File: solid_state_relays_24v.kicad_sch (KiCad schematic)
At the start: 65 parts, among them J1 1190297, J2 1190297, J3 1190297, J4 1190297, J5 1190297, J6 1190297, J7 1190297, J8 1190297, Q1 IRF4905PBF, Q2 IRF4905PBF, Q3 IRF4905PBF, Q4 IRF4905PBF, Q5 IRF4905PBF, Q6 IRF4905PBF, Q7 IRF4905PBF, Q8 IRF4905PBF

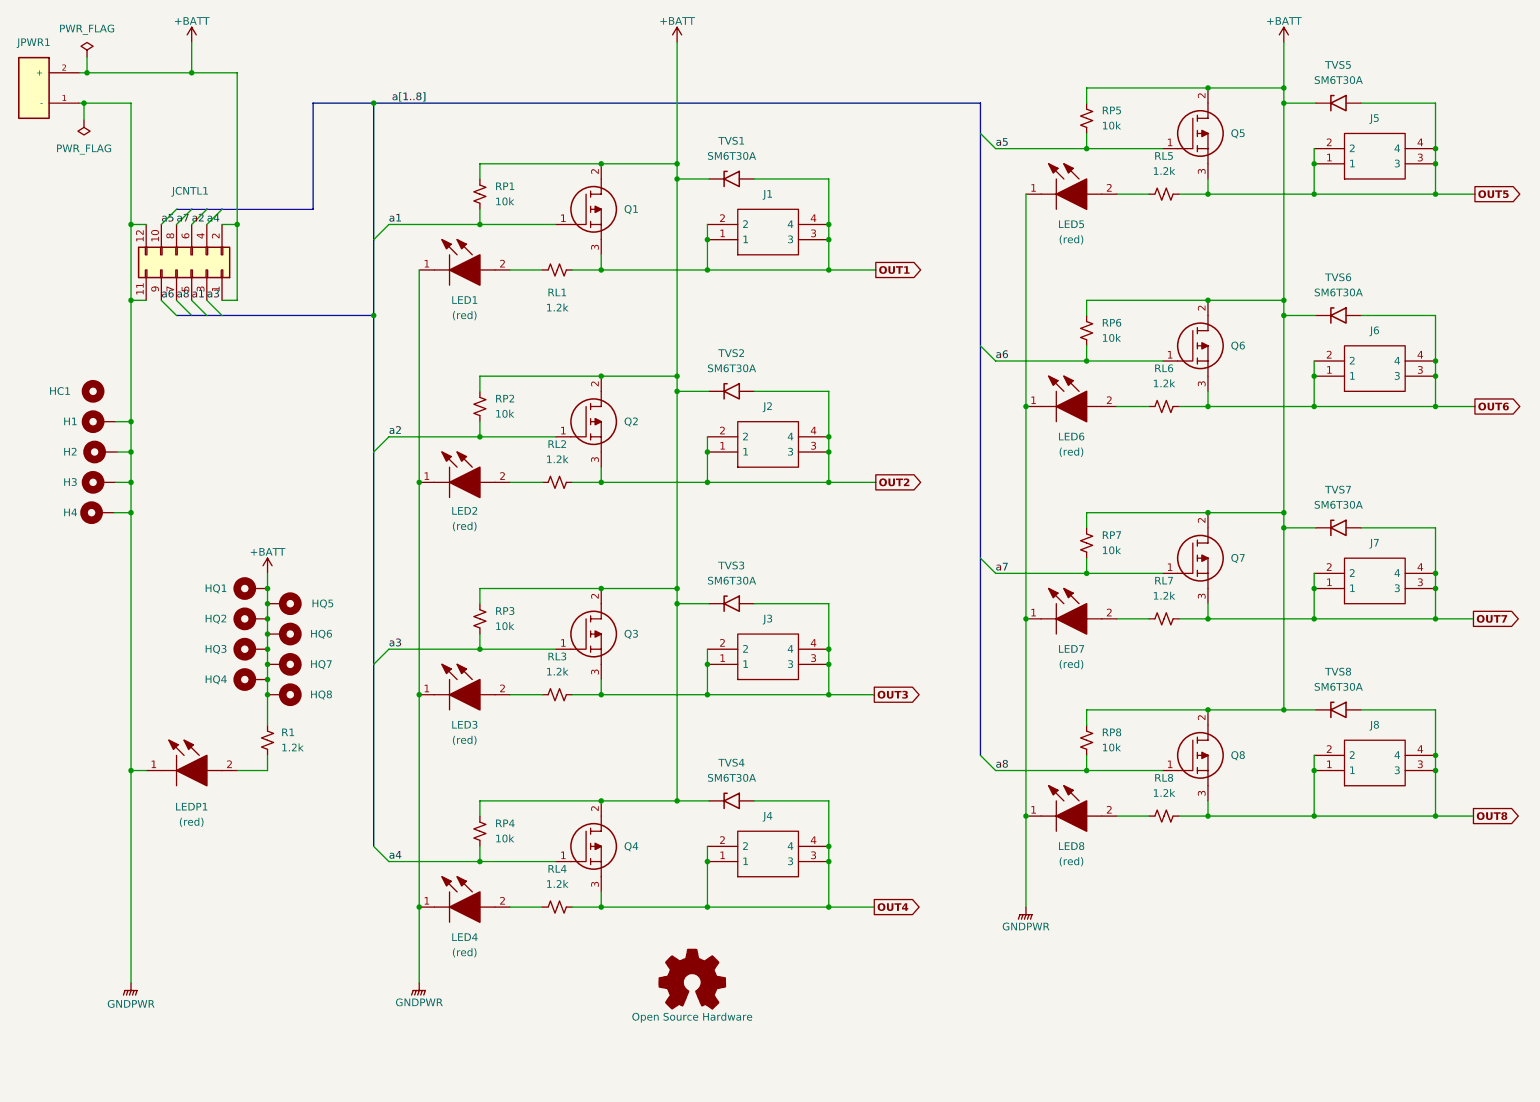
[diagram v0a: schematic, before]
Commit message: Total redo on schematic for v0.0.8
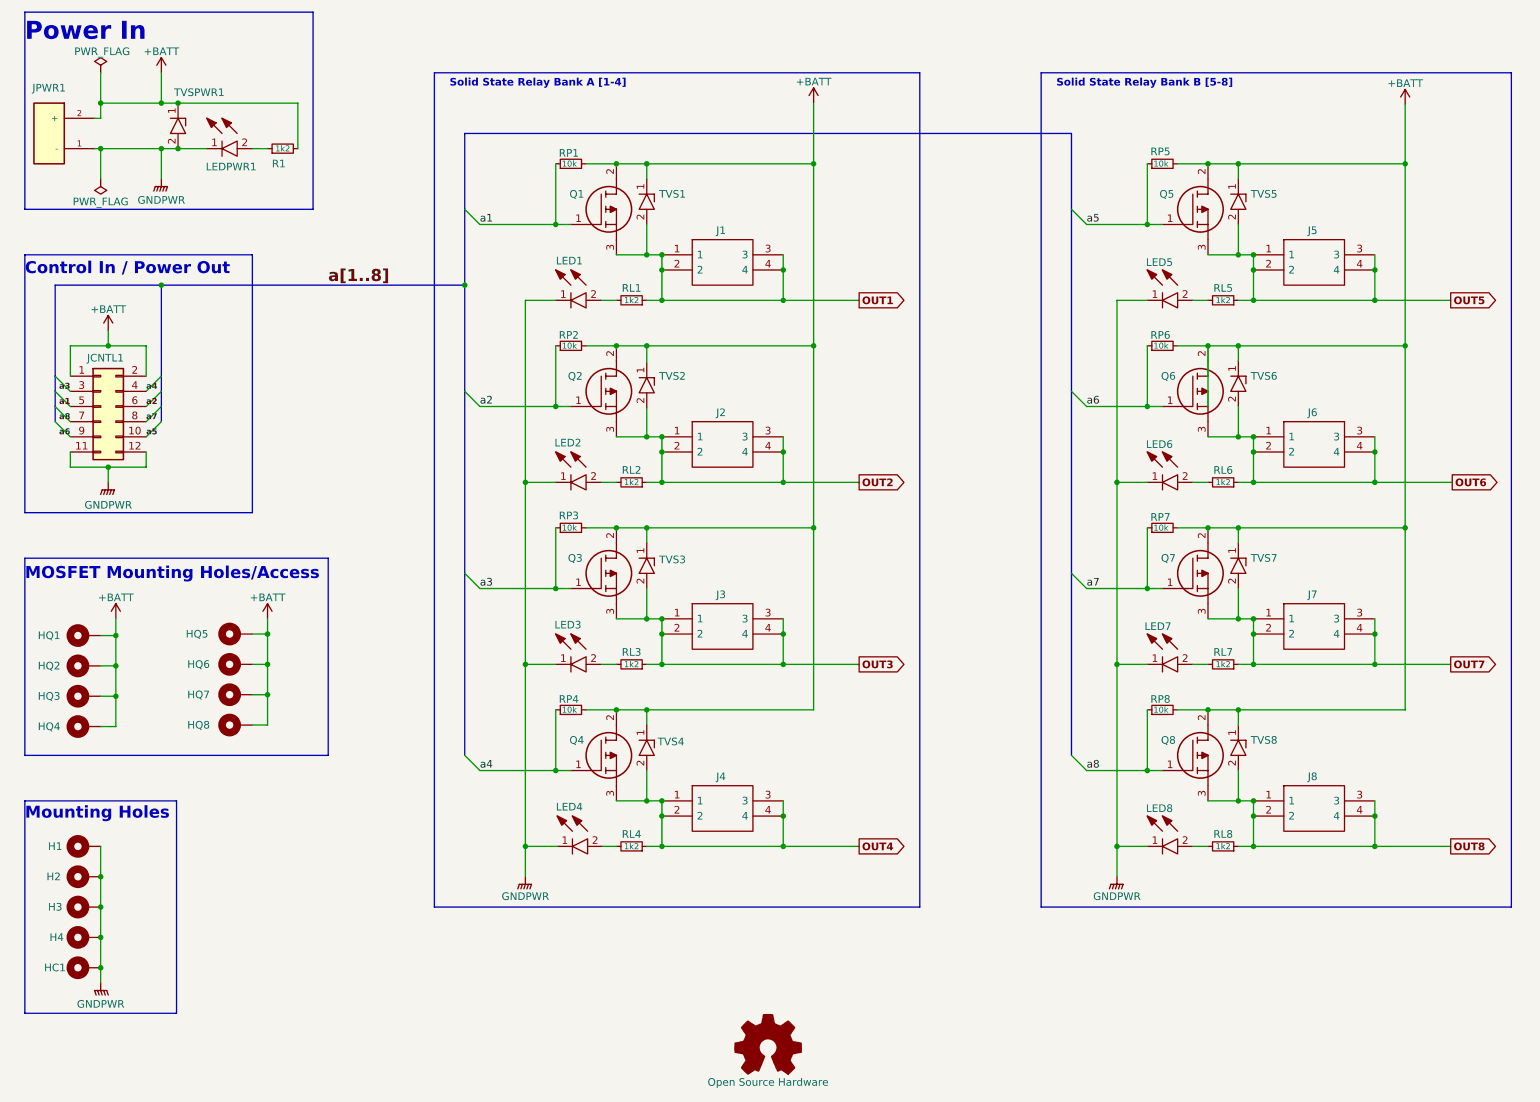
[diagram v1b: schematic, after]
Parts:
- removed J2, J3, J4, J5, J6, J7, J8: 1190297, Connector_Pheonix_Other:1190297, symbol SamacSys_Parts:1190297
- removed LED2, LED3, LED4, LED5, LED6, LED7, LED8, LEDP1: (red), SamacSys_Parts:LEDC2012X120N, symbol SamacSys_Parts:LTST-C170KRKT
- removed R1, RL2, RL3, RL4, RL5, RL6, RL7, RL8: 1.2k, Resistor_SMD:R_0805_2012Metric, symbol Device:R_Small_US
- removed RP2, RP3, RP4, RP5, RP6, RP7, RP8: 10k, Resistor_SMD:R_0805_2012Metric, symbol Device:R_Small_US
- removed TVS2, TVS3, TVS4, TVS5, TVS6, TVS7, TVS8: SM6T30A, Diode_SMD:D_SMB, symbol Diode:SM6T30A
- added J2, J3, J4, J5, J6, J7, J8: 1190297, dragon_mobile:1190297, symbol dragon_mobile:1190297
- added LED2, LED3, LED4, LED5, LED6, LED7, LED8: LTST-C190KFKT, dragon_mobile:LEDC1607X80N, symbol dragon_mobile:LTST-C190KFKT
- added LEDPWR1: LTST-C190KGKT, dragon_mobile:LEDC1608X80N, symbol dragon_mobile:LTST-C190KGKT
- added R1: 1k2, Resistor_SMD:R_0603_1608Metric_Pad0.98x0.95mm_HandSolder, symbol Device:R_Small
- added RL2, RL3, RL4, RL5, RL6, RL7, RL8: 1k2, Resistor_SMD:R_0805_2012Metric, symbol Device:R_Small
- added RP2, RP3, RP4, RP5, RP6, RP7, RP8: 10k, Resistor_SMD:R_0805_2012Metric, symbol Device:R_Small
- added TVS2, TVS3, TVS4, TVS5, TVS6, TVS7, TVS8, TVSPWR1: SM6T30AY, dragon_mobile:SMBJ36CATR, symbol dragon_mobile:SM6T30AY
- HC1: symbol Mechanical:MountingHole -> Mechanical:MountingHole_Pad
- J1: footprint Connector_Pheonix_Other:1190297 -> dragon_mobile:1190297; symbol SamacSys_Parts:1190297 -> dragon_mobile:1190297
- JCNTL1: MPN 78207-106HLF -> 78207-1012HLF; Mouser Part Number 649-78207-106HLF -> 649-78207-112HLF
- JPWR1: footprint Dragon:Amass_XT60PW-M_Kombifootprint -> dragon_mobile:Amass_XT60PW-M_Kombifootprint
- LED1: value (red) -> LTST-C190KFKT; footprint SamacSys_Parts:LEDC2012X120N -> dragon_mobile:LEDC1607X80N; symbol SamacSys_Parts:LTST-C170KRKT -> dragon_mobile:LTST-C190KFKT; Height 1.2 -> 0.8; Manufacturer_Part_Number LTST-C170KRKT -> LTST-C190KFKT; Mouser Part Number 859-LTST-C170KRKT -> 859-LTST-C190KFKT; Mouser Price/Stock https://www.mouser.com/ProductDetail/Lite-On/LTST-C170KRKT?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 -> https://www.mouser.com/ProductDetail/Lite-On/LTST-C190KFKT?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
- Q1, Q2, Q3, Q4, Q5, Q6, Q7, Q8: footprint SamacSys_Parts:TO254P469X1042X1967-3P -> dragon_mobile:TO254P469X1042X1967-3P
- RL1: value 1.2k -> 1k2; symbol Device:R_Small_US -> Device:R_Small
- RP1: symbol Device:R_Small_US -> Device:R_Small
- TVS1: value SM6T30A -> SM6T30AY; footprint Diode_SMD:D_SMB -> dragon_mobile:SMBJ36CATR; symbol Diode:SM6T30A -> dragon_mobile:SM6T30AY; Height (none) -> 2.65; Manufacturer_Name (none) -> STMicroelectronics; Manufacturer_Part_Number (none) -> SM6T30AY; Mouser Part Number (none) -> 511-SM6T30AY; Mouser Price/Stock (none) -> https://www.mouser.com/ProductDetail/STMicroelectronics/SM6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
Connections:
- net +BATT: now also RP1.2, R1.2, RP2.2, RP3.2, RP4.2, RP5.2, RP6.2, RP7.2, RP8.2, TVS2.1, TVS3.1, TVS4.1, TVS5.1, TVS6.1, TVS7.1, TVS8.1, TVSPWR1.1; no longer RP1.1
- net GNDPWR: now also HC1.1, LED2.1, LED3.1, LED4.1, LED5.1, LED6.1, LED7.1, LED8.1, LEDPWR1.1, TVSPWR1.2
- net OUT1: now also RL1.1; no longer RL1.2
- net OUT2: now also J2.1, J2.2, J2.3, J2.4, RL2.1, TVS2.2
- net OUT3: now also J3.1, J3.2, J3.3, J3.4, RL3.1, TVS3.2
- net OUT4: now also J4.1, J4.2, J4.3, J4.4, RL4.1, TVS4.2
- net OUT5: now also J5.1, J5.2, J5.3, J5.4, RL5.1, TVS5.2
- net OUT6: now also J6.1, J6.2, J6.3, J6.4, RL6.1, TVS6.2
- net OUT7: now also J7.1, J7.2, J7.3, J7.4, RL7.1, TVS7.2
- net OUT8: now also J8.1, J8.2, J8.3, J8.4, RL8.1, TVS8.2
- net a1: now also RP1.1; no longer RP1.2
- net a2: now also RP2.1
- net a3: now also RP3.1
- net a4: now also RP4.1
- net a5: now also RP5.1
- net a6: now also RP6.1
- net a7: now also RP7.1
- net a8: now also RP8.1
- net at LED1.2: now also RL1.2; no longer RL1.1
- new net: LED2.2, RL2.2
- new net: LED3.2, RL3.2
- new net: LED6.2, RL6.2
- new net: LED8.2, RL8.2
- new net: LED5.2, RL5.2
- new net: LEDPWR1.2, R1.1
- new net: LED7.2, RL7.2
- new net: LED4.2, RL4.2
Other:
- note added: "Control In / Power Out"
- note added: "MOSFET Mounting Holes/Access"
- note added: "Mounting Holes"
- note added: "Power In"
- note added: "Solid State Relay Bank A [1-4]"
- note added: "Solid State Relay Bank B [5-8]"
- moved on the sheet: H1, H2, H3, H4, HQ1, HQ2, HQ3, HQ4, HQ5, HQ6, HQ7, HQ8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

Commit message: Updating schematic and PCB for v0.0.8
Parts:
- renumbered LEDPWR1 to LEDP1, TVSPWR1 to TVSP1
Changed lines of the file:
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@@
   (symbol (lib_id "dragon_mobile:SM6T30AY") (at 40.894 30.48 270) (unit 1)
     (in_bom yes) (on_board yes)
-    (property "Reference" "TVSPWR1" (id 0) (at 44.45 28.702 90))
+    (property "Reference" "TVSP1" (id 0) (at 44.45 28.702 90))
     (property "Value" "SM6T30AY" (id 1) (at 43.434 30.48 0)
       (effects (font (size 1.27 1.27)) (justify left) hide)
@@
   (symbol (lib_id "dragon_mobile:LTST-C190KGKT") (at 45.72 38.1 0) (unit 1)
     (in_bom yes) (on_board yes)
-    (property "Reference" "LEDPWR1" (id 0) (at 49.784 41.148 0))
+    (property "Reference" "LEDP1" (id 0) (at 49.784 41.148 0))
     (property "Value" "LTST-C190KGKT" (id 1) (at 48.2346 30.48 0)
       (effects (font (size 1.27 1.27)) hide)
@@
     )
     (path "/ab793da5-b061-43cb-877a-4a6d90ef81c7"
-      (reference "LEDPWR1") (unit 1) (value "LTST-C190KGKT") (footprint "dragon_mobile:LEDC1608X80N")
+      (reference "LEDP1") (unit 1) (value "LTST-C190KGKT") (footprint "dragon_mobile:LEDC1608X80N")
     )
     (path "/1bbd3b22-5cf6-47d1-ab8c-da8e17c71421"
@@
     )
     (path "/3e9feb08-284e-450e-b0f5-20bdc79d8989"
-      (reference "TVSPWR1") (unit 1) (value "SM6T30AY") (footprint "dragon_mobile:SMBJ36CATR")
-    )
-  )
+      (reference "TVSP1") (unit 1) (value "SM6T30AY") (footprint "dragon_mobile:SMBJ36CATR")
+    )
+  )

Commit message: v0.0.10-pre2
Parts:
- added JP1: SolderJumper_2_Bridged, Jumper:SolderJumper-2_P1.3mm_Bridged_RoundedPad1.0x1.5mm, symbol Jumper:SolderJumper_2_Bridged
- added TVSP2: SM6T30AY, dragon_mobile:SMBJ36CATR, symbol dragon_mobile:SM6T30AY
- H1, H2, H3, H4, HC1, HQ1, HQ2, HQ3, HQ4, HQ5, HQ6, HQ7, HQ8: now left out of the parts list
- JPWR1: value XT60PW-M_Kombifootprint -> XT60PW-M; footprint dragon_mobile:Amass_XT60PW-M_Kombifootprint -> dragon_mobile:XT60PWM; symbol Connector_Amass_XT:XT60-M -> dragon_mobile:XT60PW-M; Height (none) -> 8.4; Manufacturer_Name (none) -> Changzou Amass Elec; Manufacturer_Part_Number (none) -> XT60PW-M; URL https://hackaday.io/page/6674-amass-xt60pw-m-combination-fo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 -> (none)
- Q1, Q2, Q3, Q4, Q5, Q6, Q7, Q8: symbol SamacSys_Parts:IRF4905PBF -> dragon_mobile:IRF4905PBF
- R1: value 1k2 -> 1k5; footprint Resistor_SMD:R_0603_1608Metric_Pad0.98x0.95mm_HandSolder -> dragon_mobile:RESC2012X65N; symbol Device:R_Small -> dragon_mobile:SDR10EZPJ152; Height (none) -> 0.65; Manufacturer_Name (none) -> ROHM Semiconductor; Manufacturer_Part_Number (none) -> SDR10EZPJ152; Mouser Part Number (none) -> 755-SDR10EZPJ152; Mouser Price/Stock (none) -> https://www.mouser.com/ProductDetail/ROHM-Semiconductor/SDR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
- RL1, RL2, RL3, RL4, RL5, RL6, RL7, RL8: value 1k2 -> 1k5; footprint Resistor_SMD:R_0805_2012Metric -> dragon_mobile:RESC2012X65N; symbol Device:R_Small -> dragon_mobile:SDR10EZPJ152; Height (none) -> 0.65; Manufacturer_Name (none) -> ROHM Semiconductor; Manufacturer_Part_Number (none) -> SDR10EZPJ152; Mouser Part Number (none) -> 755-SDR10EZPJ152; Mouser Price/Stock (none) -> https://www.mouser.com/ProductDetail/ROHM-Semiconductor/SDR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
- RP1, RP2, RP3, RP4, RP5, RP6, RP7, RP8: footprint Resistor_SMD:R_0805_2012Metric -> dragon_mobile:RESC2012X65N
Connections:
- net +BATT: now also JPWR1.P, JP1.1 (A), TVSP2.1; no longer JPWR1.2 (+), R1.2
- net GNDPWR: now also JPWR1.N, TVSP2.2; no longer JPWR1.1 (-)
- new net: JP1.2 (B), R1.2
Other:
- moved on the sheet: LEDP1, TVSP1

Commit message: WIP
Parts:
- JCNTL1: Manufacturer Amphenol FCI -> (none); Manufacturer_Name (none) -> Amphenol FCI
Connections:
- net a1: now also JCNTL1.4 (Pin_4); no longer JCNTL1.5 (Pin_5)
- net a2: now also JCNTL1.3 (Pin_3); no longer JCNTL1.6 (Pin_6)
- net a3: now also JCNTL1.6 (Pin_6); no longer JCNTL1.3 (Pin_3)
- net a4: now also JCNTL1.5 (Pin_5); no longer JCNTL1.4 (Pin_4)
- net a5: now also JCNTL1.7 (Pin_7); no longer JCNTL1.10 (Pin_10)
- net a6: now also JCNTL1.8 (Pin_8); no longer JCNTL1.9 (Pin_9)
- net a7: now also JCNTL1.9 (Pin_9); no longer JCNTL1.8 (Pin_8)
- net a8: now also JCNTL1.10 (Pin_10); no longer JCNTL1.7 (Pin_7)
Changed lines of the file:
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@@
     (effects (font (size 3 3) bold) (justify left bottom))
   )
-  (label "a5" (at 35.56 86.36 0)
+  (label "a8" (at 35.56 86.36 0)
     (effects (font (size 1 1) (thickness 0.2) bold) (justify left bottom))
   )
-  (label "a4" (at 35.56 78.74 0)
+  (label "a1" (at 35.56 78.74 0)
     (effects (font (size 1 1) (thickness 0.254) bold) (justify left bottom))
   )
-  (label "a6" (at 22.86 86.36 180)
+  (label "a7" (at 22.86 86.36 180)
     (effects (font (size 1 1) (thickness 0.2) bold) (justify right bottom))
   )
-  (label "a8" (at 22.86 83.82 180)
+  (label "a5" (at 22.86 83.82 180)
     (effects (font (size 1 1) (thickness 0.2) bold) (justify right bottom))
   )
@@
     (effects (font (size 1.27 1.27)) (justify left bottom))
   )
-  (label "a1" (at 22.86 81.28 180)
+  (label "a4" (at 22.86 81.28 180)
     (effects (font (size 1 1) (thickness 0.2) bold) (justify right bottom))
   )
-  (label "a3" (at 22.86 78.74 180)
+  (label "a2" (at 22.86 78.74 180)
     (effects (font (size 1 1) (thickness 0.2) bold) (justify right bottom))
   )
@@
     (effects (font (size 1.27 1.27)) (justify left bottom))
   )
-  (label "a7" (at 35.56 83.82 0)
+  (label "a6" (at 35.56 83.82 0)
     (effects (font (size 1 1) (thickness 0.2) bold) (justify left bottom))
   )
-  (label "a2" (at 35.56 81.28 0)
+  (label "a3" (at 35.56 81.28 0)
     (effects (font (size 1 1) (thickness 0.2) bold) (justify left bottom))
   )
@@
       (effects (font (size 1.27 1.27)) hide)
     )
-    (property "Datasheet" "~" (id 3) (at 106.68 40.64 0)
+    (property "Datasheet" "" (id 3) (at 106.68 40.64 0)
       (effects (font (size 1.27 1.27)) hide)
     )
@@
       (effects (font (size 1.27 1.27)) (justify left) hide)
     )
-    (property "Manufacturer" "Amphenol FCI" (id 5) (at 29.21 110.49 0)
-      (effects (font (size 1.27 1.27)) (justify left) hide)
-    )
     (property "Mouser Part Number" "649-78207-112HLF" (id 6) (at 29.21 97.79 0)
       (effects (font (size 1.27 1.27)) (justify left) hide)
     )
-    (pin "1")
+    (property "Manufacturer_Name" "Amphenol FCI" (id 7) (at 27.94 81.28 0)
+      (effects (font (size 1.27 1.27)) hide)
+    )
+    (pin "1")
